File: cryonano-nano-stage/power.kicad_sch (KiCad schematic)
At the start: 32 parts, among them Q1 PMV100EPAR, U4 AP7363-33D-13

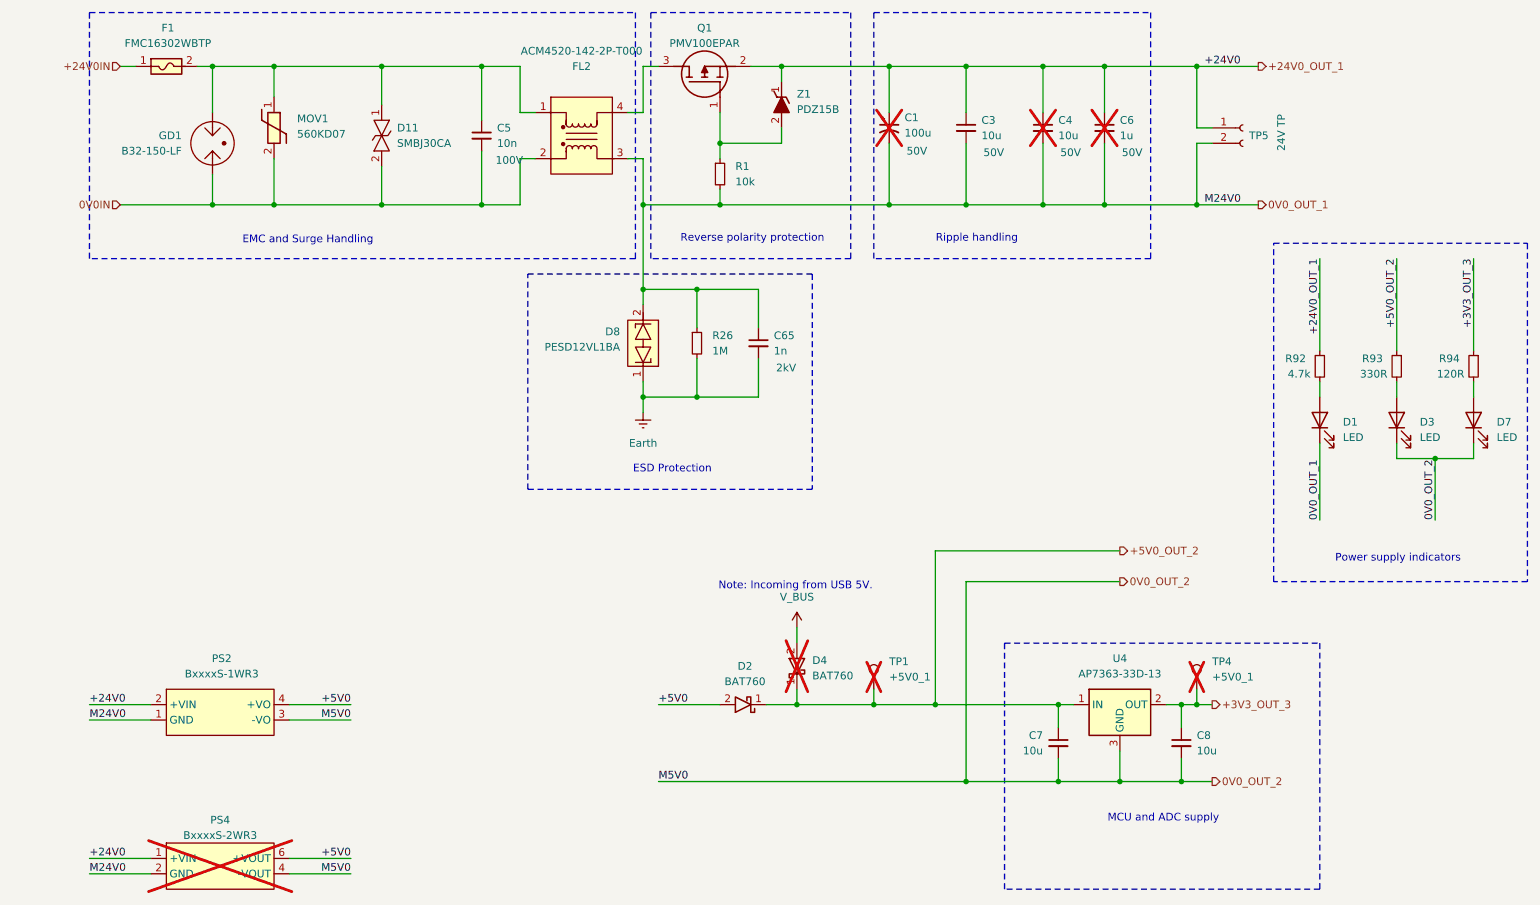
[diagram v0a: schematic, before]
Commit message: bom adjusted
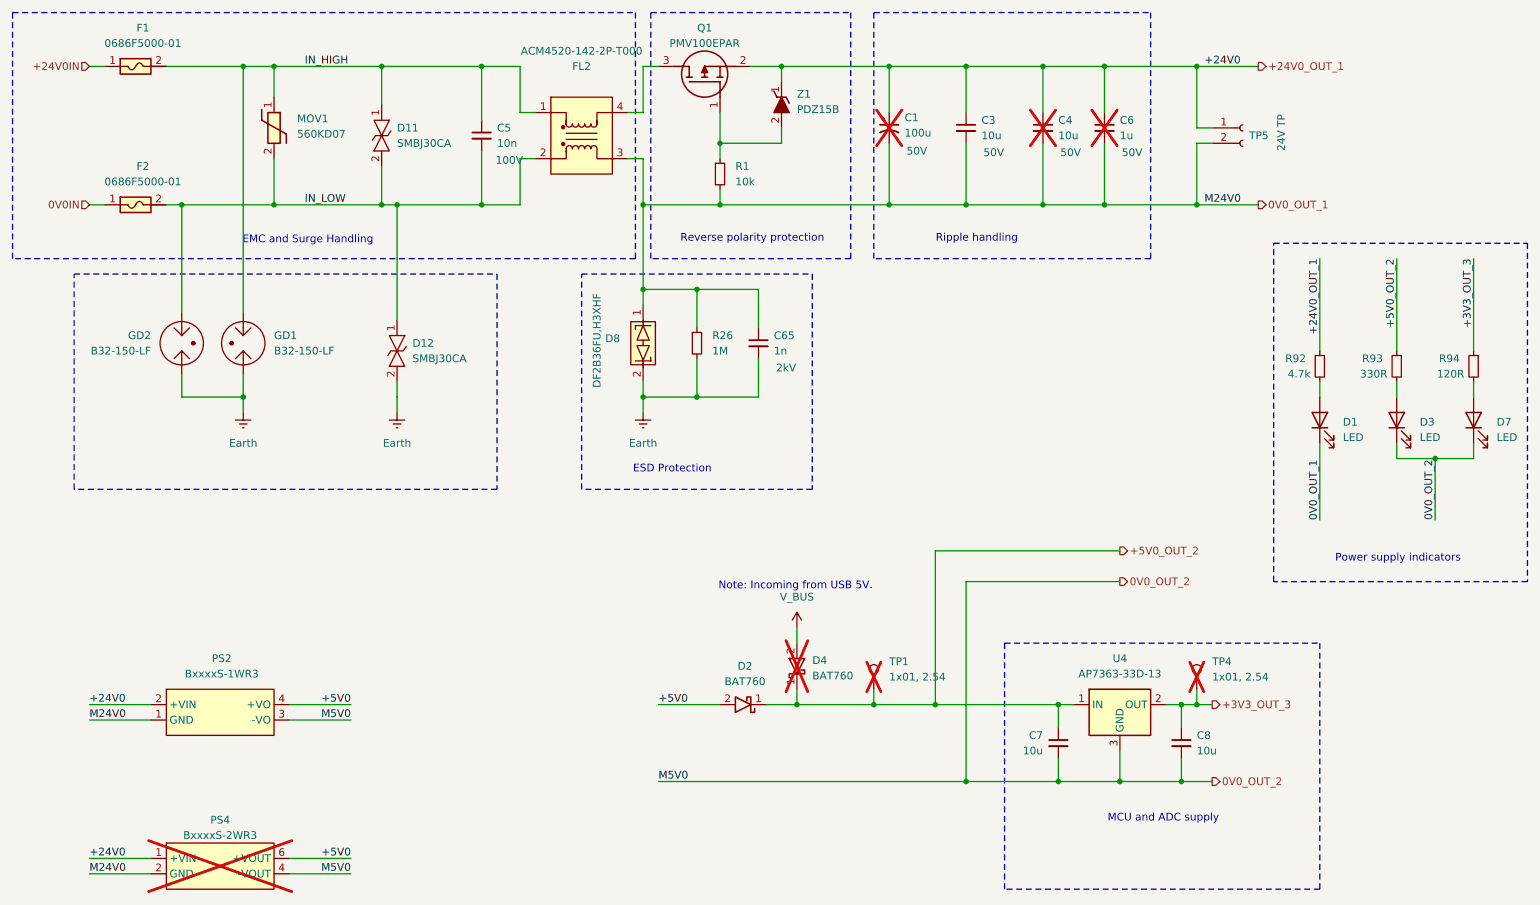
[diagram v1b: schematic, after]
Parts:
- removed D8: PESD12VL1BA, Diode_SMD:D_SOD-323F, symbol symbols:PESD12VL1BA,115
- removed F1: FMC16302WBTP, footprints:FUSC1608X55N, symbol symbols:FMC16302WBTP
- added D12: SMBJ30CA, Diode_SMD:D_SMB, symbol symbols:SMBJ30CA/TR13
- added D8: DF2B36FU,H3XHF, Diode_SMD:D_SOD-323, symbol symbols:DF2B36FU
- added F1, F2: 0686F5000-01, Fuse:Fuse_0603_1608Metric, symbol symbols:0686F5000-01
- added GD2: B32-150-LF, footprints:B32_GDT_YAGEO, symbol symbols:B32-150-LF
- D1: Order No. (none) -> LED_RED
- D3: Order No. (none) -> LED_YELLOW
- D7: Order No. (none) -> LED_GREEN
- R1, R92, R93, R94: Order No. (none) -> 0603/120mW
- R26: Order No. (none) -> LR1F1M0
- TP1, TP4: value +5V0_1 -> 1x01, 2.54; Order No. (none) -> N.A.
- TP5: value 1x02 2.54mm -> 1x02, 2.54; Order No. (none) -> N.A.
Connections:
- net +24V0IN: now also F1.1
- net 0V0IN: now also F2.1; no longer C5.2, D11.2, FL2.2, GD1.2, MOV1.2
- net 0V0_OUT_1: now also D8.1
- net Earth: now also GD1.2, D12.2, D8.2, GD2.2
- net IN_HIGH: now reaches C5.1, D11.1, FL2.1, GD1.1, MOV1.1
- net IN_HIGH: now also F1.2
- new net IN_LOW: C5.2, D11.2, D12.1, F2.2, FL2.2, GD2.1, MOV1.2
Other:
- moved on the sheet: GD1

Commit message: drc ok, review schematic
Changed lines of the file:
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@@
-	)
-	(rectangle
-		(start 35.56 68.58)
-		(end 105.41 104.14)
-		(stroke
-			(width 0.1524)
-			(type dash)
-		)
-		(fill
-			(type none)
-		)
 	)
 	(rectangle
@@
 	)
 	(rectangle
-		(start 119.38 68.58)
+		(start 33.02 68.58)
 		(end 157.48 104.14)
 		(stroke
@@
 	(text "ESD Protection"
 		(exclude_from_sim no)
-		(at 134.366 100.838 0)
+		(at 103.886 101.6 0)
 		(effects
 			(font

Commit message: sch reviewed
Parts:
- added R30: 2.7k, Resistor_SMD:R_0805_2012Metric, symbol Device:R_Small
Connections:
- net +5V0: now also R30.2
- net 0V0_OUT_2: now also R30.1
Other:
- moved on the sheet: TP5

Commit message: release candidate
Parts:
- R1, R92, R93, R94: Order No. 0603/120mW -> 0603, 120mW
- R30: Order No. 0805/225mW -> 0805, 225mW
- TP1, TP4: Source N.A -> (none)
- TP5: Comment 24V TP -> (none)
